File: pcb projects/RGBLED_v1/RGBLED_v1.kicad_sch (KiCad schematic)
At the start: 26 parts, among them CN1 USB_B_Micro, CN2 Conn_01x03_Pin, J1 Conn_02x02_Odd_Even, SW1 SW_MEC_5E, U1 STM32F091RBTx, U2 LP3985IM5-3.3/NOPB, Y1 32.768kHz

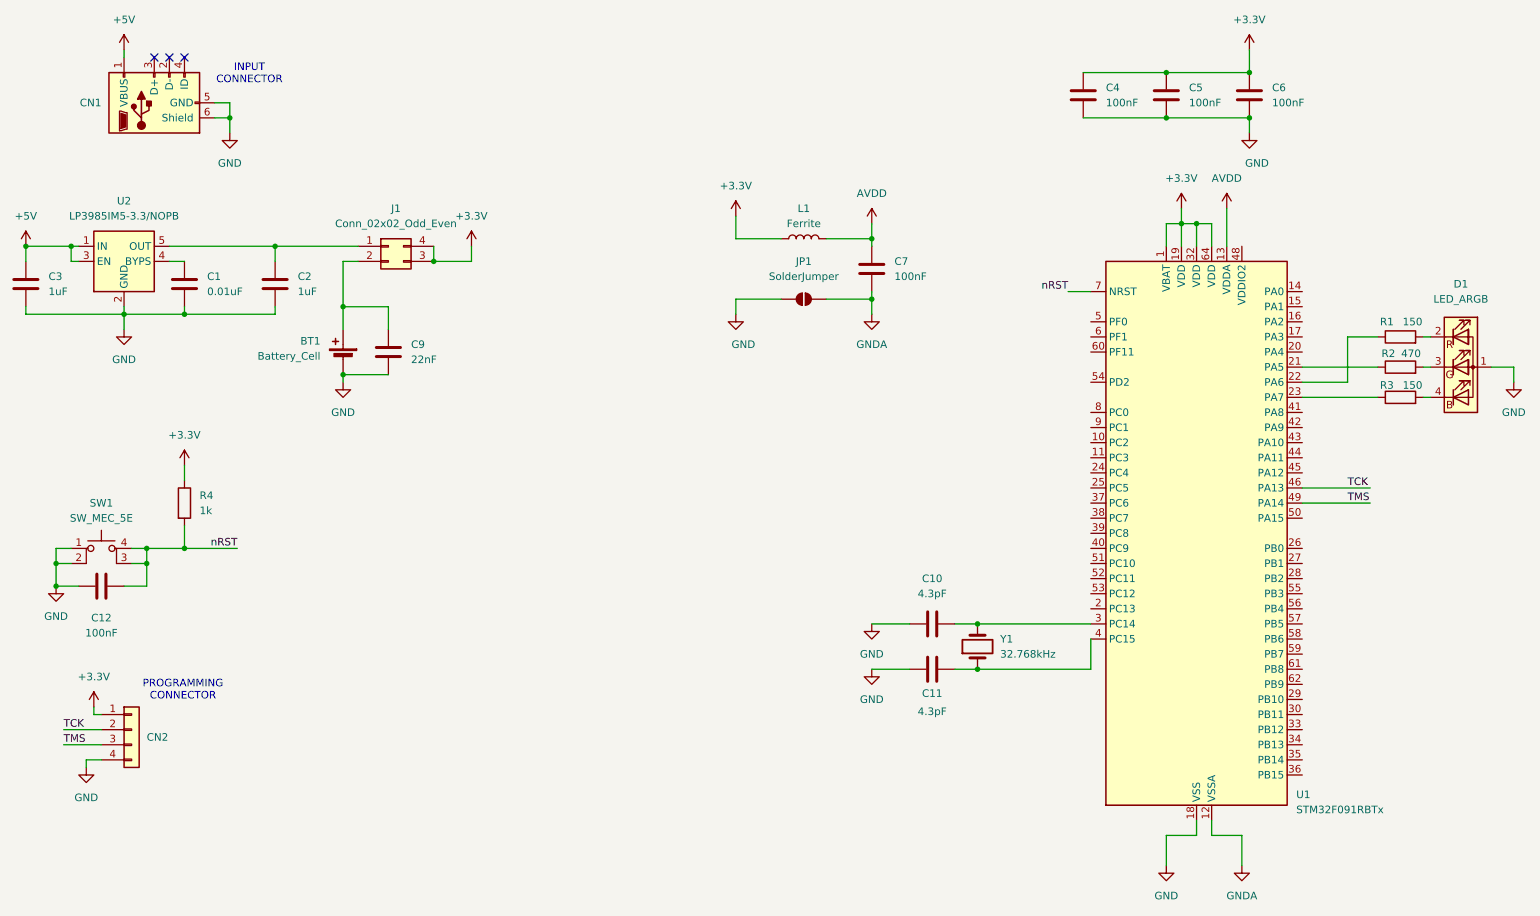
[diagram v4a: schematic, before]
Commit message: comp changes: stab to tht, cap to tantal; fixed comp placing on pcb
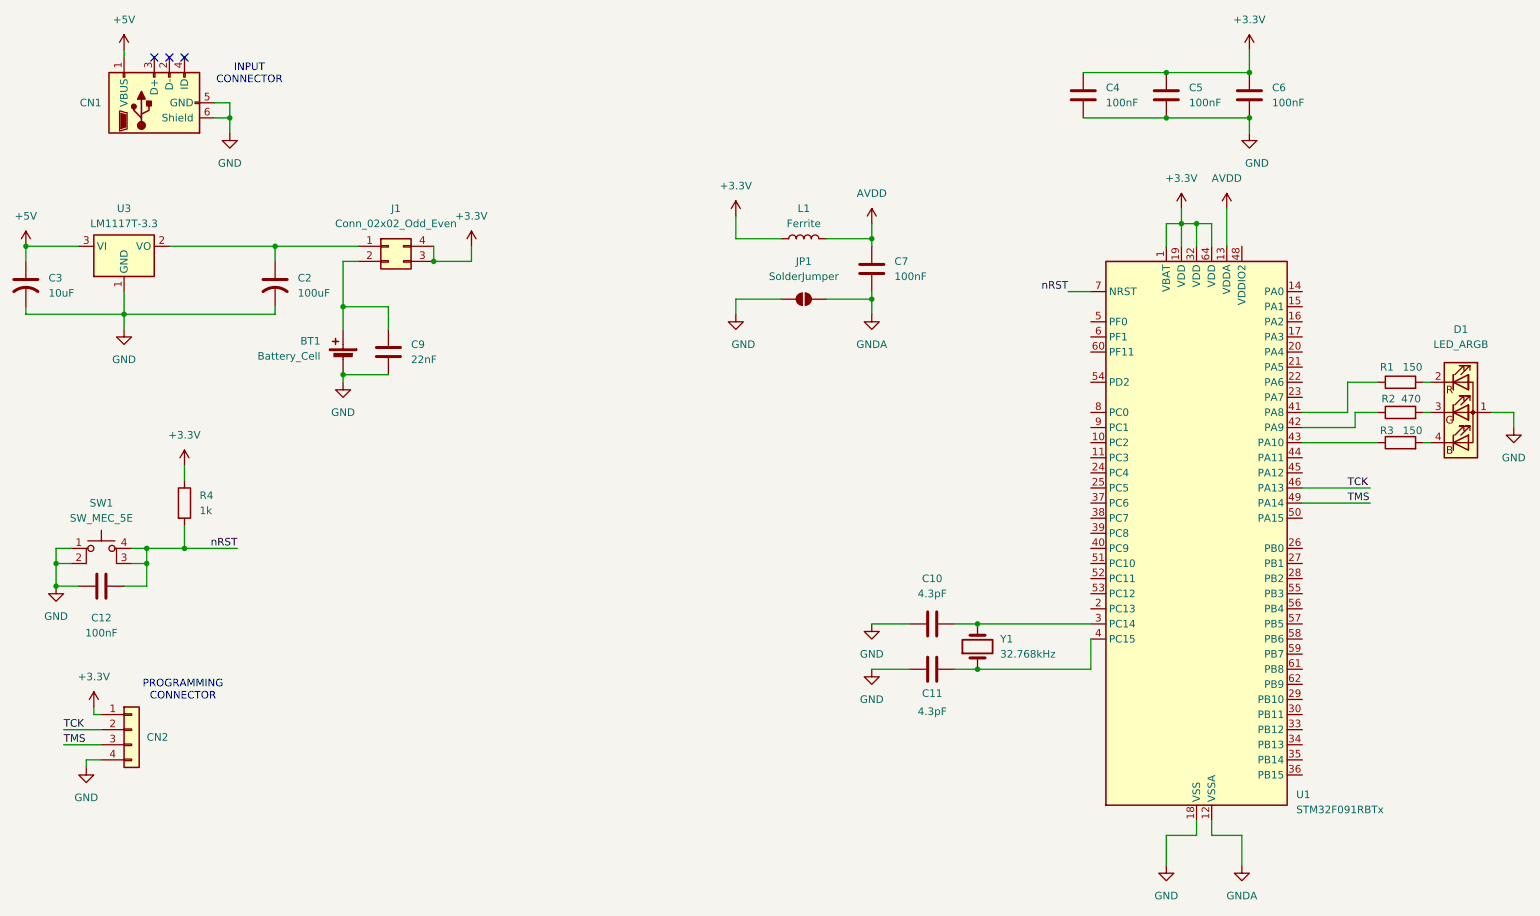
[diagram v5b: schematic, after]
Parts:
- removed C1: 0.01uF, Capacitor_SMD:C_1206_3216Metric_Pad1.33x1.80mm_HandSolder, symbol Device:C
- removed U2: LP3985IM5-3.3/NOPB, Package_TO_SOT_SMD:SOT-23-5, symbol Regulator_Linear:LP3987H-33B5
- added U3: LM1117T-3.3, Package_TO_SOT_THT:TO-220-3_Vertical, symbol Regulator_Linear:LM1117T-3.3
- C12: footprint (none) -> Capacitor_Tantalum_SMD:CP_EIA-3528-21_Kemet-B_HandSolder
- C2: value 1uF -> 100uF; footprint Capacitor_SMD:C_1206_3216Metric_Pad1.33x1.80mm_HandSolder -> Capacitor_Tantalum_SMD:CP_EIA-3528-21_Kemet-B_HandSolder; symbol Device:C -> Device:C_US
- C3: value 1uF -> 10uF; footprint Capacitor_SMD:C_1206_3216Metric_Pad1.33x1.80mm_HandSolder -> Capacitor_Tantalum_SMD:CP_EIA-3528-21_Kemet-B_HandSolder; symbol Device:C -> Device:C_US
- L1: footprint (none) -> Inductor_SMD:L_0603_1608Metric_Pad1.05x0.95mm_HandSolder
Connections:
- net +5V: now also U3.3 (VI)
- net GND: now also U3.1 (GND)
- net at U1.21 (PA5): no longer R2.1
- net at U1.22 (PA6): no longer R1.1
- net at U1.23 (PA7): no longer R3.1
- net at U1.41 (PA8): now also R1.1
- net at U1.42 (PA9): now also R2.1
- net at U1.43 (PA10): now also R3.1
- net at C2.1, J1.1 (Pin_1): now also U3.2 (VO)
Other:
- moved on the sheet: D1, R1, R2, R3

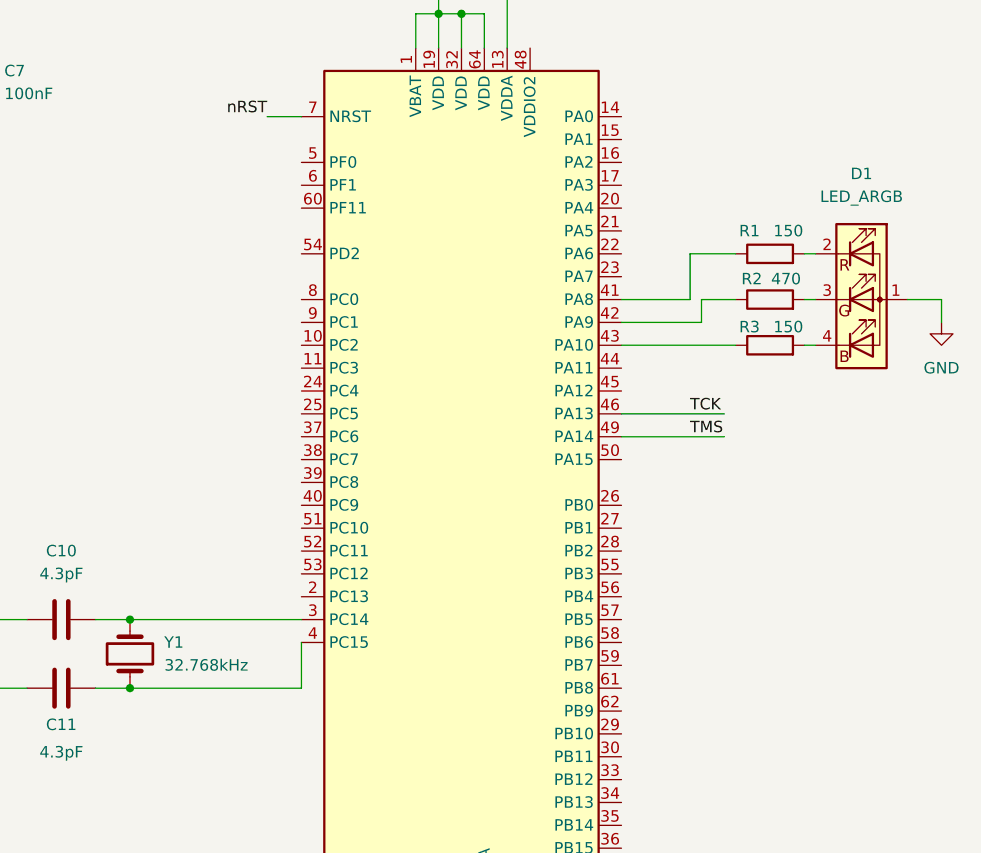
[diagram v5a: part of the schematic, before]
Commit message: D1 sch fix, stab fix, gnd zone fixed, started verification and BOM
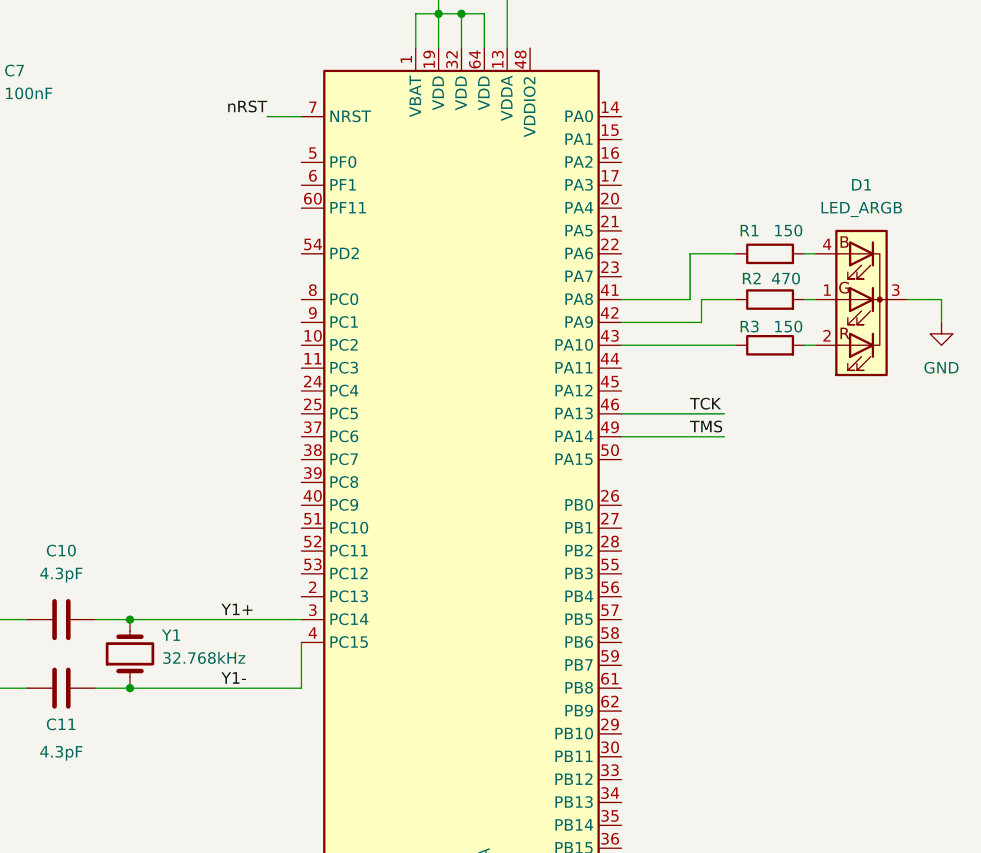
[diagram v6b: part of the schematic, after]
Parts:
- D1: symbol Device:LED_ARGB -> Device:LED_KRGB
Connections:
- net GND: now also D1.3 (GA); no longer D1.1 (A)
- net Y1+: now reaches C10.2, U1.3 (PC14), Y1.2
- net Y1-: now reaches C11.1, U1.4 (PC15), Y1.1
- net at R2.2: now also D1.1 (K); no longer D1.3 (GK)
- net at R3.2: now also D1.2 (RA); no longer D1.4 (BK)
- net at R1.2: now also D1.4 (BA); no longer D1.2 (RK)
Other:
- moved on the sheet: D1
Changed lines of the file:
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@@
+		)
+	)
+	(label "Y1-"
+		(at 194.31 125.73 0)
+		(effects
+			(font
+				(size 1.27 1.27)
+			)
+			(justify left bottom)
+		)
+	)
+	(label "Y1+"
+		(at 194.31 118.11 0)
+		(effects
+			(font
+				(size 1.27 1.27)
+			)
+			(justify left bottom)
 		)
 	)
@@
 		(on_board yes)
 		(dnp no)
-		(fields_autoplaced yes)
 		(property "Reference" "Y1"
-			(at 187.96 120.6499 90)
+			(at 187.706 119.888 90)
 			(effects
 				(font
@@
 		)
 		(property "Value" "32.768kHz"
-			(at 187.96 123.1899 90)
+			(at 187.706 122.428 90)
 			(effects
 				(font
@@
 	)
 	(symbol
-		(lib_id "Device:LED_ARGB")
-		(at 265.43 82.55 0)
+		(lib_id "Device:LED_KRGB")
+		(at 265.43 82.55 180)
 		(unit 1)
 		(exclude_from_sim no)
@@
 		(fields_autoplaced yes)
 		(property "Reference" "D1"
-			(at 265.43 68.58 0)
+			(at 265.43 69.85 0)
 			(effects
 				(font
@@
 		)
 		(property "Value" "LED_ARGB"
-			(at 265.43 71.12 0)
+			(at 265.43 72.39 0)
 			(effects
 				(font
@@
 		)
 		(property "Footprint" "Connector_PinHeader_2.54mm:PinHeader_1x04_P2.54mm_Vertical"
-			(at 265.43 83.82 0)
+			(at 265.43 81.28 0)
 			(effects
 				(font
@@
 		)
 		(property "Datasheet" "~"
-			(at 265.43 83.82 0)
-			(effects
-				(font
-					(size 1.27 1.27)
-				)
-				(hide yes)
-			)
-		)
-		(property "Description" "RGB LED, anode/red/green/blue"
+			(at 265.43 81.28 0)
+			(effects
+				(font
+					(size 1.27 1.27)
+				)
+				(hide yes)
+			)
+		)
+		(property "Description" "RGB LED, cathode/red/green/blue"
 			(at 265.43 82.55 0)
 			(effects

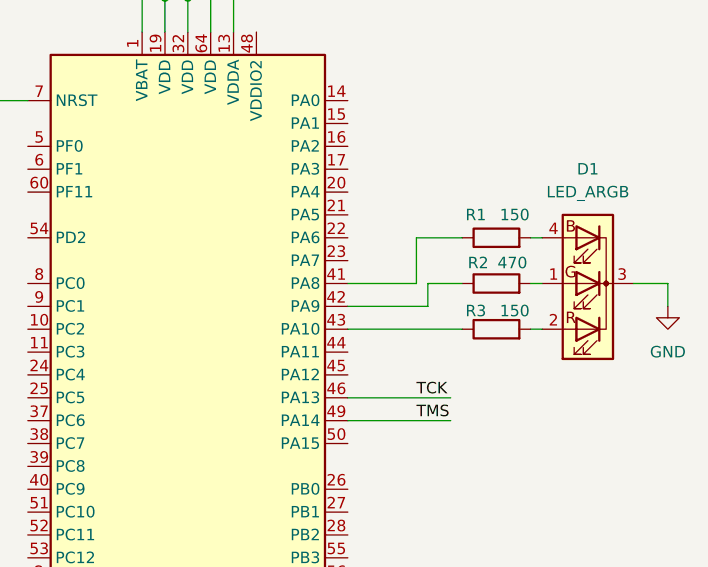
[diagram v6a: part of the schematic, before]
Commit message: title added, D1 connected
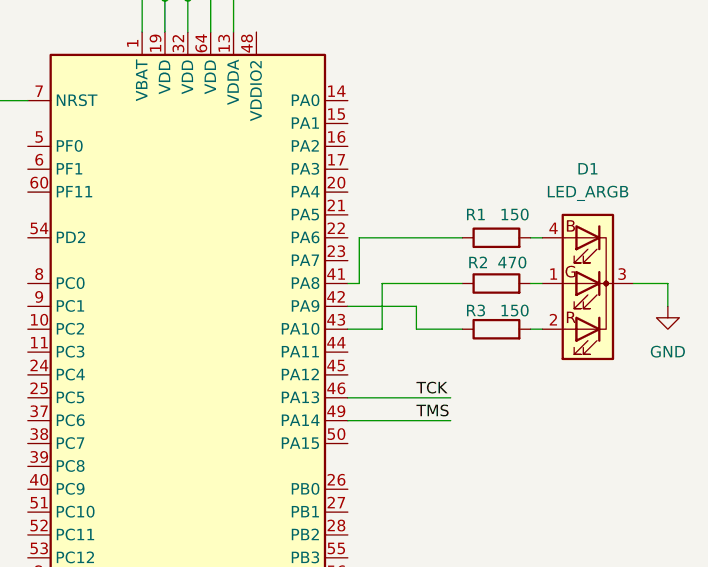
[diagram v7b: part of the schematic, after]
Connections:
- net at U1.42 (PA9): now also R3.1; no longer R2.1
- net at U1.43 (PA10): now also R2.1; no longer R3.1
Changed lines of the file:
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@@
+	(wire
+		(pts
+			(xy 251.46 82.55) (xy 242.57 82.55)
+		)
+		(stroke
+			(width 0)
+			(type default)
+		)
+	)
 	(wire
 		(pts
@@
 	(wire
 		(pts
+			(xy 242.57 82.55) (xy 242.57 87.63)
+		)
+		(stroke
+			(width 0)
+			(type default)
+		)
+	)
+	(wire
+		(pts
 			(xy 29.21 107.95) (xy 29.21 111.76)
 		)
@@
 	(wire
 		(pts
-			(xy 247.65 85.09) (xy 238.76 85.09)
+			(xy 240.03 77.47) (xy 251.46 77.47)
+		)
+		(stroke
+			(width 0)
+			(type default)
+		)
+	)
+	(wire
+		(pts
+			(xy 246.38 85.09) (xy 246.38 87.63)
 		)
 		(stroke
@@
 	(wire
 		(pts
-			(xy 247.65 82.55) (xy 247.65 85.09)
-		)
-		(stroke
-			(width 0)
-			(type default)
-		)
-	)
-	(wire
-		(pts
 			(xy 41.91 107.95) (xy 44.45 107.95)
 		)
@@
 	(wire
 		(pts
-			(xy 246.38 77.47) (xy 246.38 82.55)
-		)
-		(stroke
-			(width 0)
-			(type default)
-		)
-	)
-	(wire
-		(pts
 			(xy 44.45 105.41) (xy 50.8 105.41)
 		)
@@
 	(wire
 		(pts
-			(xy 238.76 82.55) (xy 246.38 82.55)
-		)
-		(stroke
-			(width 0)
-			(type default)
-		)
-	)
-	(wire
-		(pts
 			(xy 29.21 105.41) (xy 29.21 107.95)
 		)
@@
 	(wire
 		(pts
-			(xy 251.46 82.55) (xy 247.65 82.55)
-		)
-		(stroke
-			(width 0)
-			(type default)
-		)
-	)
-	(wire
-		(pts
 			(xy 259.08 87.63) (xy 260.35 87.63)
 		)
@@
 	(wire
 		(pts
-			(xy 246.38 77.47) (xy 251.46 77.47)
-		)
-		(stroke
-			(width 0)
-			(type default)
-		)
-	)
-	(wire
-		(pts
 			(xy 229.87 33.02) (xy 229.87 35.56)
 		)
@@
 	(wire
 		(pts
+			(xy 246.38 87.63) (xy 251.46 87.63)
+		)
+		(stroke
+			(width 0)
+			(type default)
+		)
+	)
+	(wire
+		(pts
 			(xy 24.13 54.61) (xy 24.13 57.15)
 		)
@@
 	(wire
 		(pts
+			(xy 238.76 82.55) (xy 240.03 82.55)
+		)
+		(stroke
+			(width 0)
+			(type default)
+		)
+	)
+	(wire
+		(pts
 			(xy 85.09 64.77) (xy 77.47 64.77)
 		)
@@
 	(wire
 		(pts
+			(xy 242.57 87.63) (xy 238.76 87.63)
+		)
+		(stroke
+			(width 0)
+			(type default)
+		)
+	)
+	(wire
+		(pts
 			(xy 85.09 68.58) (xy 85.09 64.77)
 		)
@@
 	(wire
 		(pts
+			(xy 238.76 85.09) (xy 246.38 85.09)
+		)
+		(stroke
+			(width 0)
+			(type default)
+		)
+	)
+	(wire
+		(pts
 			(xy 66.04 54.61) (xy 80.01 54.61)
 		)
@@
 	(wire
 		(pts
+			(xy 240.03 82.55) (xy 240.03 77.47)
+		)
+		(stroke
+			(width 0)
+			(type default)
+		)
+	)
+	(wire
+		(pts
 			(xy 226.06 48.26) (xy 226.06 54.61)
 		)
@@
 		)
 		(stroke
-			(width 0)
-			(type default)
-		)
-	)
-	(wire
-		(pts
-			(xy 251.46 87.63) (xy 238.76 87.63)
-		)
-		(stroke
